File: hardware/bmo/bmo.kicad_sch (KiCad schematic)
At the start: 0 parts

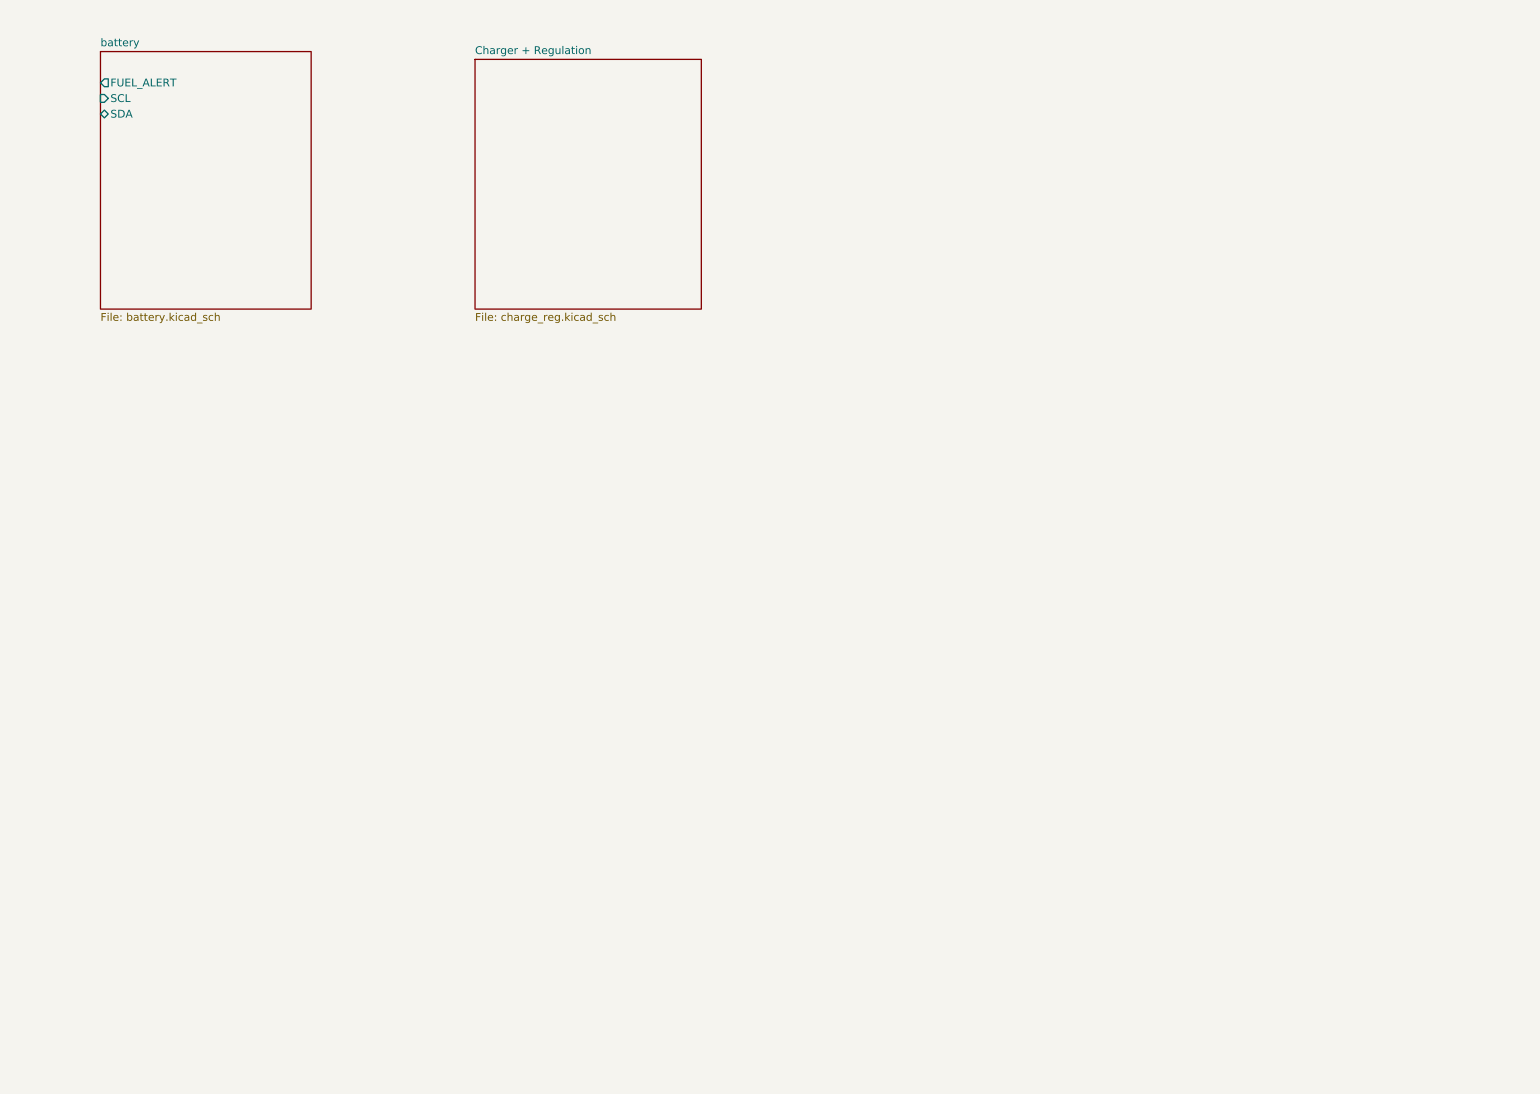
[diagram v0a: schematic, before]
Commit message: Placed and routed everything. DRC is clean.
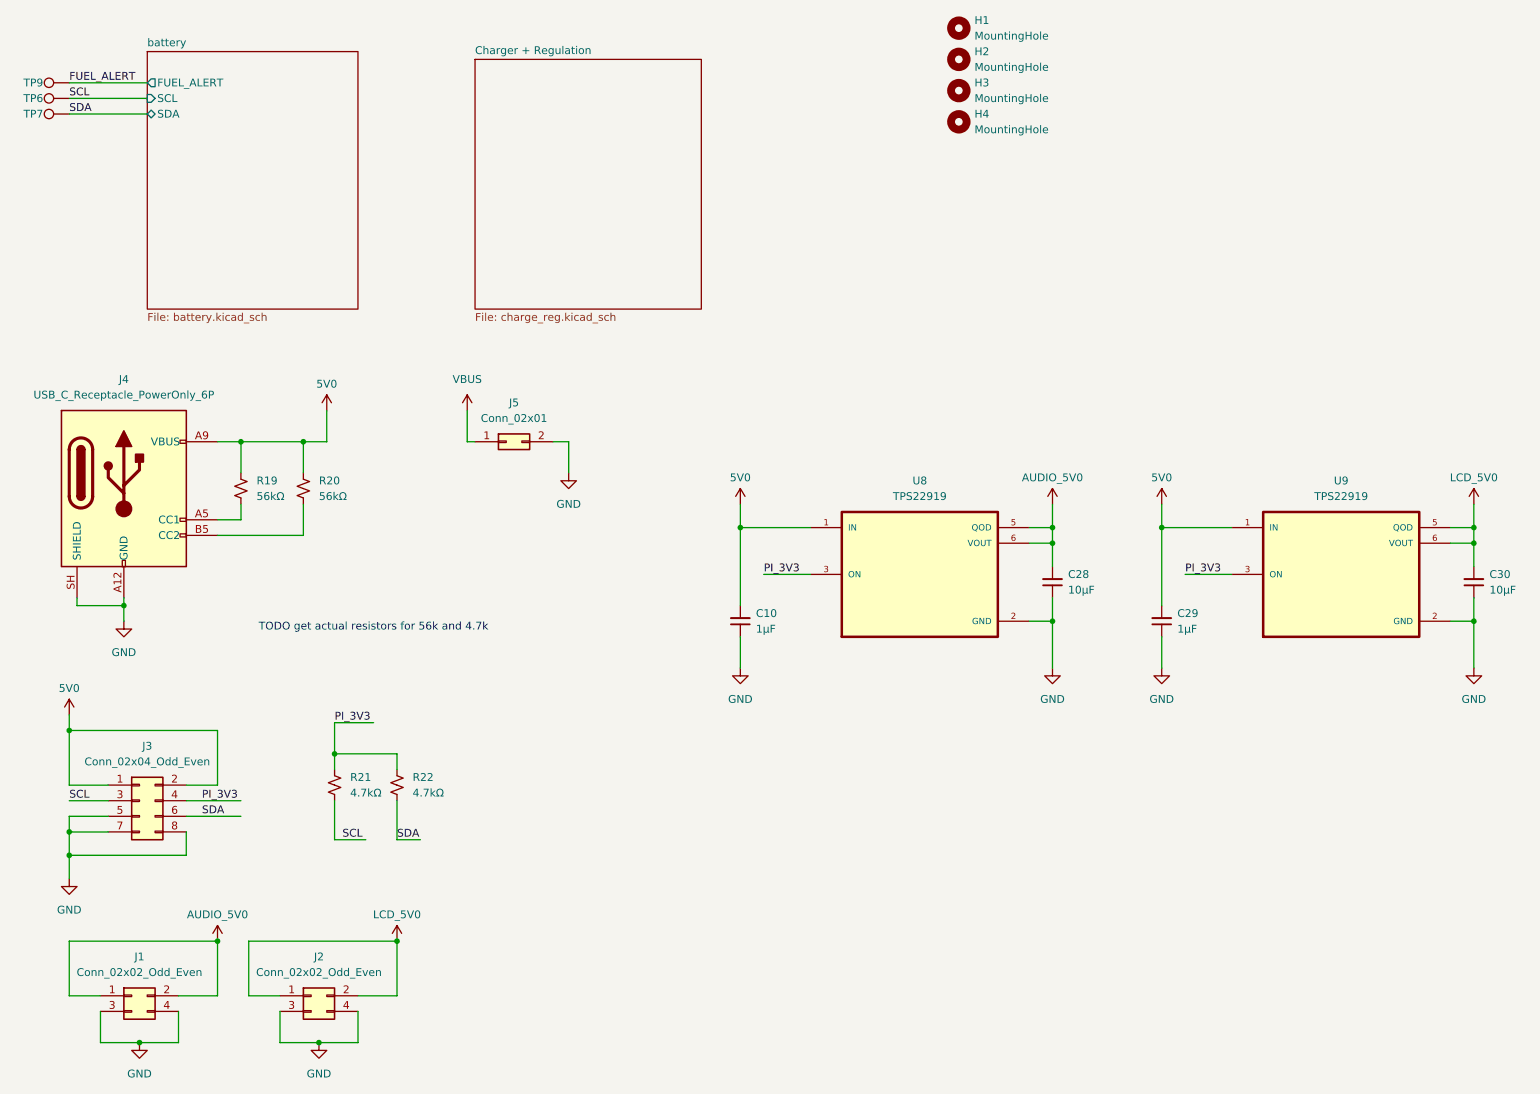
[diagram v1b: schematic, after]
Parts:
- added C10, C29: 1µF, Capacitor_SMD:C_0402_1005Metric_Pad0.74x0.62mm_HandSolder, symbol Device:C_Small
- added C28, C30: 10µF, Capacitor_SMD:C_0402_1005Metric_Pad0.74x0.62mm_HandSolder, symbol Device:C_Small
- added H1, H2, H3, H4: MountingHole, MountingHole:MountingHole_2.7mm_M2.5, symbol Mechanical:MountingHole
- added J1, J2: Conn_02x02_Odd_Even, Connector_PinHeader_2.54mm:PinHeader_2x02_P2.54mm_Vertical, symbol Connector_Generic:Conn_02x02_Odd_Even
- added J3: Conn_02x04_Odd_Even, Connector_PinHeader_2.54mm:PinHeader_2x04_P2.54mm_Vertical, symbol Connector_Generic:Conn_02x04_Odd_Even
- added J4: USB_C_Receptacle_PowerOnly_6P, Connector_USB:USB_C_Receptacle_GCT_USB4125-xx-x-0190_6P_TopMnt_Horizontal, symbol Connector:USB_C_Receptacle_PowerOnly_6P
- added J5: Conn_02x01, Connector_PinSocket_2.54mm:PinSocket_2x01_P2.54mm_Vertical, symbol Connector_Generic:Conn_02x01
- added R19, R20: 56kΩ, Resistor_SMD:R_0402_1005Metric_Pad0.72x0.64mm_HandSolder, symbol Device:R_Small_US
- added R21, R22: 4.7kΩ, Resistor_SMD:R_0402_1005Metric_Pad0.72x0.64mm_HandSolder, symbol Device:R_Small_US
- added TP6, TP7, TP9: TestPoint, TestPoint:TestPoint_Pad_2.0x2.0mm, symbol Connector:TestPoint
- added U8, U9: TPS22919, Package_TO_SOT_SMD:SOT-363_SC-70-6, symbol bmo:TPS22919
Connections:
- new net: J4.A5 (CC1), R19.2
- new net: J4.B5 (CC2), R20.2
- new net 5V0: C10.2, C29.2, J3.1 (Pin_1), J3.2 (Pin_2), J4.A9 (VBUS), J4.B9 (VBUS), R19.1, R20.1, U8.1 (IN), U9.1 (IN)
- new net AUDIO_5V0: C28.2, J1.1 (Pin_1), J1.2 (Pin_2), U8.5 (QOD), U8.6 (VOUT)
- new net FUEL_ALERT: TP9.1
- new net GND: C10.1, C28.1, C29.1, C30.1, J1.3 (Pin_3), J1.4 (Pin_4), J2.3 (Pin_3), J2.4 (Pin_4), J3.5 (Pin_5), J3.7 (Pin_7), J3.8 (Pin_8), J4.A12 (GND), J4.B12 (GND), J4.SH (SHIELD), J5.2 (Pin_2), U8.2 (GND), U9.2 (GND)
- new net LCD_5V0: C30.2, J2.1 (Pin_1), J2.2 (Pin_2), U9.5 (QOD), U9.6 (VOUT)
- new net PI_3V3: J3.4 (Pin_4), R21.1, R22.1, U8.3 (ON), U9.3 (ON)
- new net SCL: J3.3 (Pin_3), R21.2, TP6.1
- new net SDA: J3.6 (Pin_6), R22.2, TP7.1
- new net VBUS: J5.1 (Pin_1)
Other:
- note added: "TODO get actual resistors for 56k and 4.7k"
